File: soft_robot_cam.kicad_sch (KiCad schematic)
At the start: 87 parts, among them J1 Connector, J10 Screw_Terminal_01x02, J11 Conn_02x02_Counter_Clockwise, J2 Conn_01x06, J3 Conn_01x03, J4 Conn_01x05_Pin, J5 Conn_01x02_Pin, J6 Screw_Terminal_01x02, J7 Screw_Terminal_01x02, J8 Conn_01x24_Socket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

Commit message: Cleaned Up BOM
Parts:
- F1: value JFC1206-1450FS -> BHFUSE BSMD1206C-1700T; LCSC (none) -> C41367230
- J11: LCSC C41370696 -> C22438179
- J8: footprint Connector_FFC-FPC:Hirose_FH12-24S-0.5SH_1x24-1MP_P0.50mm_Horizontal -> easyeda2kicad:FPC-SMD_AFC07-S24ECA-00
- L1: footprint easyeda2kicad:IND-SMD_L6.0-W6.0_SRN6045 -> easyeda2kicad:IND-SMD_L6.0-W6.0; LCSC C42370386 -> C341066; LCSC Part C42261 -> (none); Name SWPA6028S6R8MT -> (none)
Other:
- moved on the sheet: R25

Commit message: Critical Fixes
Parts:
- removed TP1: TestPoint_2Pole, symbol Connector:TestPoint_2Pole
- added TP4: TestPoint_2Pole, symbol Connector:TestPoint_2Pole
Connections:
- net CS1: now also U9.32 (IO39); no longer U9.31 (IO38)
- net GND: now also R25.1, TP4.1; no longer R25.2
- net I2C_SCL: now also R3.2, TP3.2, U9.15 (IO3); no longer R24.2, U9.16 (IO46)
- net I2C_SDA: now also R24.2, U9.14 (IO20), TP4.2; no longer R3.2, TP3.2, U9.15 (IO3)
- net IN1_A: now also U9.28 (IO35); no longer R25.1, U9.26 (IO45)
- net LDR2: now also U9.16 (IO46); no longer U9.14 (IO20)
- net MISO1: now also U9.31 (IO38); no longer U9.30 (IO37)
- net MOSI1: now also U9.29 (IO36); no longer U9.28 (IO35)
- net SCLK1: now also U9.30 (IO37); no longer U9.29 (IO36)
- net TOF_INT: no longer U9.33 (IO40)
- net XSHUT: now also U9.33 (IO40); no longer U9.32 (IO39)
- new net: R25.2, U9.26 (IO45)
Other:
- moved on the sheet: R25

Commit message: Fixes the layout
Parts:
- removed J2: Conn_01x06, easyeda2kicad:JST_B6B-PH-K-S, symbol Connector_Generic:Conn_01x06
- added J12: B5B-PH-K-S-(LF)(SN), easyeda2kicad:CONN-TH_B5B-PH-K-S-LF-SN, symbol easyeda2kicad:B5B-PH-K-S-(LF)(SN)
- added R26: 10kΩ, PCM_JLCPCB:R_0603, symbol PCM_JLCPCB-Resistors:0603,10kΩ
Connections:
- net XSHUT is gone; now on net nFAULT_A: U9.33 (IO40)
- net +3.3V: now also J12.1, J12.4
- net GND: now also TP4.2, J12.5, R26.1; no longer TP4.1
- net I2C_SDA: now also TP4.1; no longer TP4.2
- net LDR2: now also U9.5 (IO5); no longer U9.16 (IO46)
- net SCL: now also J12.3
- net SDA: now also J12.2
- net nFAULT_A: no longer U9.5 (IO5)
- new net: R26.2, U9.16 (IO46)
- no-connect marks 17 -> 18

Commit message: Production ready PCB
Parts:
- removed J11: Conn_02x02_Counter_Clockwise, Connector_PinHeader_1.00mm:PinHeader_2x02_P1.00mm_Vertical, symbol Connector_Generic:Conn_02x02_Counter_Clockwise
- added U1: PZ127-2-02-Z, easyeda2kicad:HDR-TH_4P-P1.27-V-M-R2-C2-S1.27_MH127V-12-04-0820, symbol easyeda2kicad:PZ127-2-02-Z
- J12: LCSC (none) -> C157993
- J8: LCSC C202112 -> C262643
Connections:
- net +3.3V: now also U3.22 (nCS), U1.1, U1.3; no longer J12.1
- net GND: now also U1.2, U1.4
- net IN1_A: now also U9.31 (IO38); no longer U9.28 (IO35)
- net SCL: now also U3.23 (SCL/SCLK)
- net SDA: now also U3.24 (SDA/SDI)
- net nFAULT_A: now also U9.32 (IO39); no longer U9.33 (IO40)
- removed net CS1: U3.22 (nCS), U9.32 (IO39)
- net MISO1: no longer names the net of U3.9 (SDO/AD0)
- net MISO1: no longer U9.31 (IO38)
- net MOSI1: no longer names the net of U9.29 (IO36)
- net MOSI1: no longer U3.24 (SDA/SDI)
- net SCLK1: no longer names the net of U9.30 (IO37)
- net SCLK1: no longer U3.23 (SCL/SCLK)
- new net XSHUT: J12.1, U9.33 (IO40)
- no-connect marks 18 -> 22

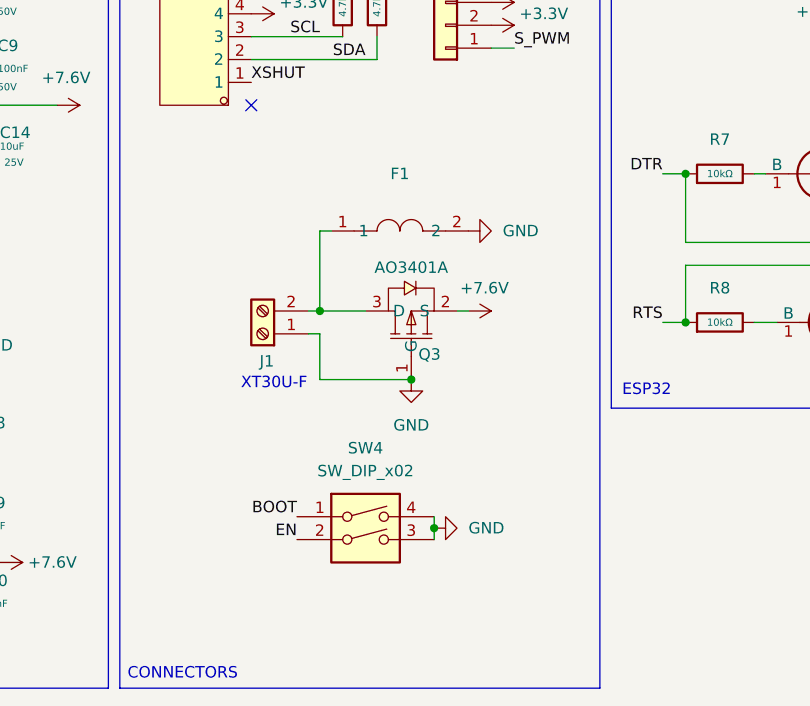
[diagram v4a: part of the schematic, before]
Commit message: Fixed Fuse, Added more testpads, changed xt30 to male, added switch in schematic for GPIO3
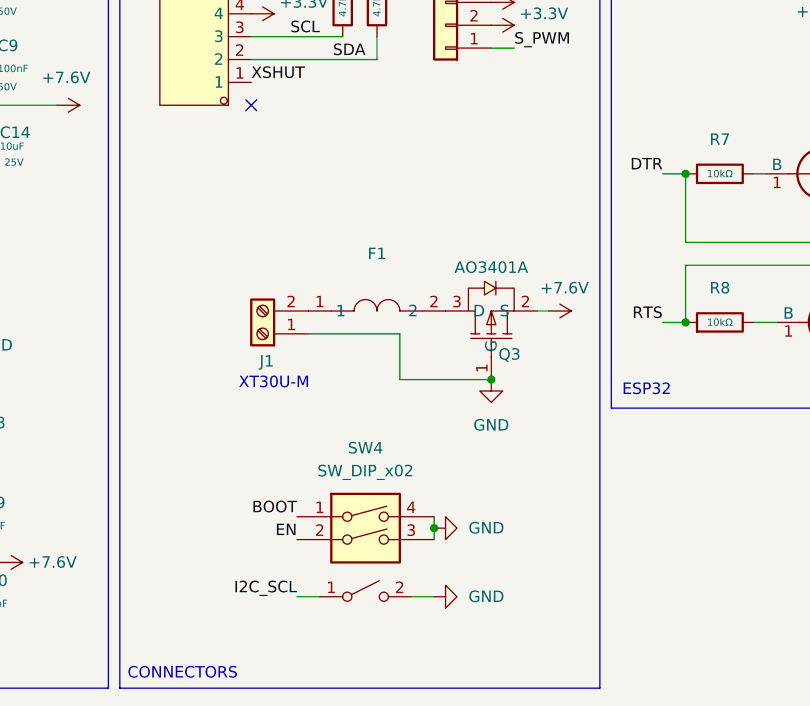
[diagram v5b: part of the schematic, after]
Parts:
- added SW1: SW_DPST_x2, symbol Switch:SW_DPST_x2
- J1: LCSC C99102 -> C99101
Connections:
- net GND: now also SW1.2 (B); no longer F1.2
- net I2C_SCL: now also SW1.1 (A)
- net at F1.1, J1.2 (Pin_2): no longer Q3.3 (D)
- new net: F1.2, Q3.3 (D)
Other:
- note added: "XT30U-M"
- note removed: "XT30U-F"
- moved on the sheet: F1, Q3
